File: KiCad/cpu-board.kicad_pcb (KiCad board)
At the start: 2 copper layers, 100 x 100 mm, 25 parts, among them CON1 BARREL_JACK, P1 CONN_01X06, SW1 SW_PUSH_SMALL, SW2 SWITCH_INV, U1 68008D, U2 XC9572XL_VQ44, U3 29F040B, U4 BS62LV4006, X1 OSCILLATOR

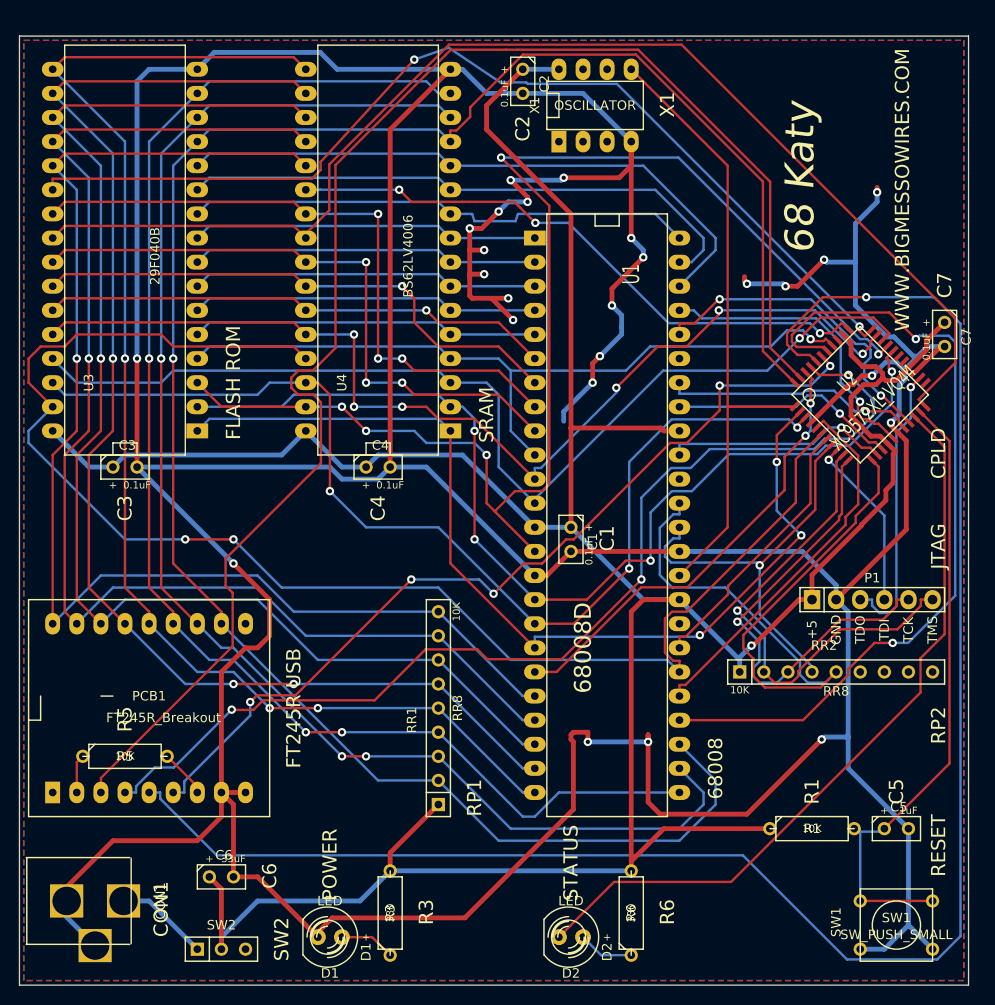
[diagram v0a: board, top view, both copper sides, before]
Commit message: add footprints to schema, add chips to board layout
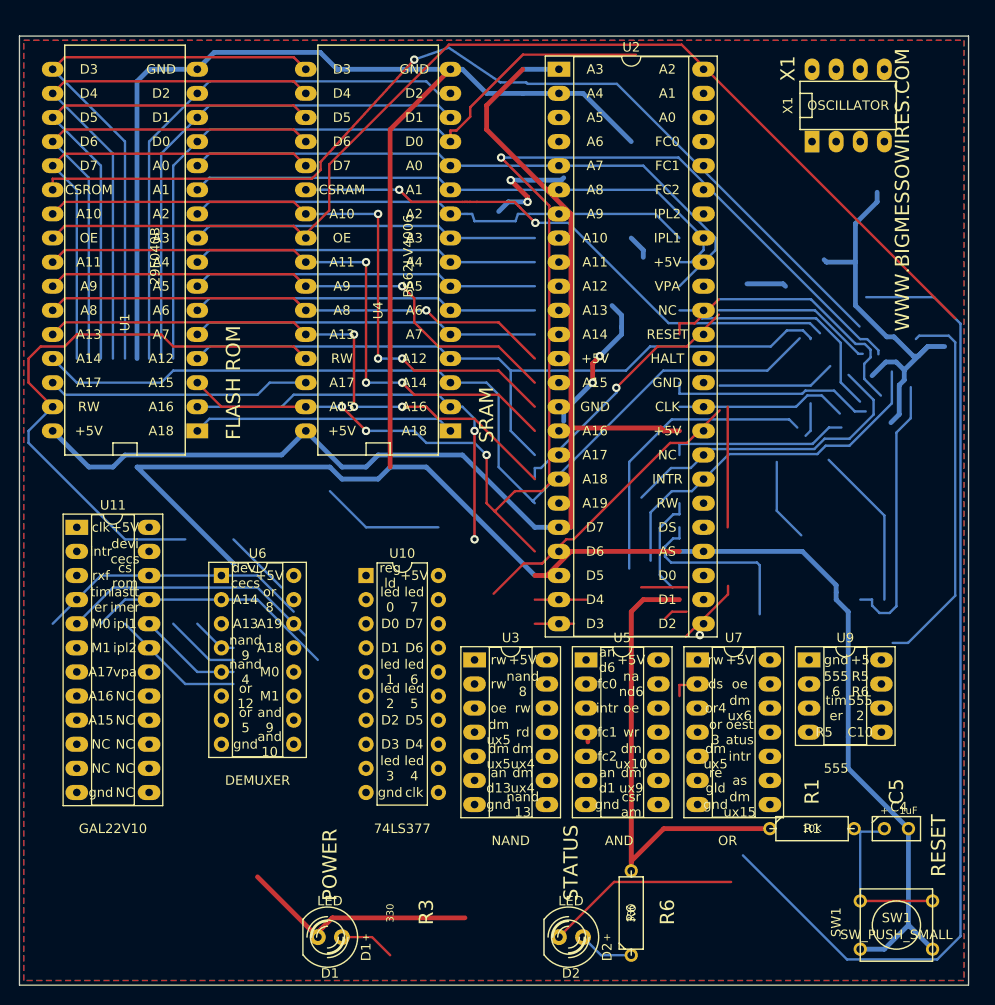
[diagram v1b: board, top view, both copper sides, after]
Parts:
- removed C1, C2, C3, C7: 0.1uF, Discret:C1
- removed the C4 at (97.8, 105.4)
- removed C6: 33uF, Discret:C1
- removed CON1: BARREL_JACK, BMOW:BMOW_BARREL_JACK
- removed P1: CONN_01X06, Pin_Headers:Pin_Header_Straight_1x06
- removed PCB1: FT245R_Breakout, BMOW:FT245_Breakout
- removed R3: 330, Discret:R3-5
- removed R5: 10K, Discret:R3-5
- removed RR1, RR2: RR8, Discret:r_pack8
- removed SW2: SWITCH_INV, Discret:MICROSWITCH_SPST
- removed the U1 at (121.9, 110.5)
- added U10: 74LS377, 68KatyClone:74LS377, F.Cu at (96.5, 116.8)
- added U11: GAL22V10, 68KatyClone:GAL22V10, F.Cu at (66.0, 111.8)
- added U3: 74LS00, 68KatyClone:DIP-14_W7.62mm_Socket_LongPads, F.Cu at (108.0, 125.7)
- added U5: 74LS08, 68KatyClone:DIP-14_W7.62mm_Socket_LongPads, F.Cu at (119.7, 125.7)
- added U6: 74LS139, 68KatyClone:74LS139, F.Cu at (81.3, 116.8)
- added U7: 74LS32, 68KatyClone:DIP-14_W7.62mm_Socket_LongPads, F.Cu at (131.4, 125.7)
- added U9: LM555, 68KatyClone:DIP-8_W7.62mm_Socket_LongPads, F.Cu at (143.2, 125.7)
- U2: value XC9572XL_VQ44 -> 68008D; footprint SMD_Packages:VQFP-44 -> 68KatyClone:DIP-48_W15.24mm_Socket_LongPads
- moved U2 46.7 mm to (116.8, 63.5), turned to 0 degrees
- moved X1 26.7 mm to (147.3, 67.3)
- renumbered C5 to C4, U3 to U1
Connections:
- C4 pad 1: /BTN -> /RESET
- R1 pad 2: /BTN -> /RESET
- SW1 pad 1: /BTN -> /RESET
- U1 pad 22: /CEROM -> /CSROM
- U2 pad 1: /CLK -> /A3
- U2 pad 10: /TMS -> /A12
- U2 pad 11: /TCK -> /A13
- U2 pad 12: /RESET -> /A14
- U2 pad 13: /VPA -> +5V
- U2 pad 14: /IPL1 -> /A15
- U2 pad 15: +5V -> GND
- U2 pad 16: /FC0 -> /A16
- U2 pad 17: GND -> /A17
- U2 pad 18: /IPL2 -> /A18
- U2 pad 19: /FC1 -> /A19
- U2 pad 2: /A18 -> /A4
- U2 pad 20: /STATUS -> /D7
- U2 pad 21: /BTN -> /D6
- U2 pad 22: /OE -> /D5
- U2 pad 23: Net-(U2-Pad23) -> /D4
- U2 pad 24: /TDO -> /D3
- U2 pad 25: GND -> /D2
- U2 pad 26: +5V -> /D1
- U2 pad 27: Net-(U2-Pad27) -> /D0
- U2 pad 28: Net-(U2-Pad28) -> /AS
- U2 pad 29: /A16 -> /DS
- U2 pad 3: /A17 -> /A5
- U2 pad 30: /A15 -> /RW
- U2 pad 31: /A14 -> /INTR
- U2 pad 32: /A13 -> Net-(U2-Pad32)
- U2 pad 33: /CEROM -> +5V
- U2 pad 34: /CERAM -> /CLK
- U2 pad 35: +5V -> GND
- U2 pad 36: Net-(U2-Pad36) -> /HALT
- U2 pad 37: /A12 -> /RESET
- U2 pad 38: /AS -> Net-(U2-Pad38)
- U2 pad 39: /RD -> /VPA
- U2 pad 4: GND -> /A6
- U2 pad 40: /WR -> +5V
- U2 pad 41: /RXF -> /IPL1
- U2 pad 42: /A19 -> /IPL2
- U2 pad 43: /TXE -> /FC2
- U2 pad 44: /D0 -> /FC1
- U2 pad 5: /DS -> /A7
- U2 pad 6: /RW -> /A8
- U2 pad 7: /DTACK -> /A9
- U2 pad 8: /HALT -> /A10
- U2 pad 9: /TDI -> /A11
- U4 pad 22: /CERAM -> /CSRAM
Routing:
- net GND: track 618.6 -> 349.5 mm, vias 25 -> 2
- net /WR: track 184.8 -> 0.00 mm, vias 1 -> 0
- net /TXE: track 160.0 -> 0.00 mm
- net /D0: track 218.9 -> 76.2 mm, vias 1 -> 0
- net +5V: track 329.1 -> 189.7 mm, vias 1 -> 0
- net /RXF: track 111.2 -> 0.00 mm, vias 3 -> 0
- net /CEROM: track 106.4 -> 0.00 mm, vias 2 -> 0
- net /CSROM: track 0.00 -> 104.1 mm, vias 0 -> 1
- net Net-(U11-Pad13): track 0.00 -> 104.1 mm
- net /D1: track 152.4 -> 54.7 mm, vias 3 -> 0
- net /RD: track 93.5 -> 0.00 mm, vias 5 -> 0
- net /D2: track 149.6 -> 57.8 mm, vias 3 -> 0
- net /D7: track 136.3 -> 49.1 mm, vias 1 -> 0
- net /D6: track 137.3 -> 52.2 mm, vias 1 -> 0
- net /D5: track 138.4 -> 55.2 mm, vias 1 -> 0
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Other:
- board text added: "+5V"
- board text added: "555"
- board text added: "555 2"
- board text added: "555 6"
- board text added: "74LS377"
- board text added: "A0"
- board text added: "A1"
- board text added: "A10"
- board text added: "A11"
- board text added: "A12"
- board text added: "A13"
- board text added: "A14"
- board text added: "A15"
- board text added: "A16"
- board text added: "A17"
- board text added: "A18"
- board text added: "A19"
- board text added: "A2"
- board text added: "A3"
- board text added: "A4"
- board text added: "A5"
- board text added: "A6"
- board text added: "A7"
- board text added: "A8"
- board text added: "A9"
- board text added: "AND"
- board text added: "AS"
- board text added: "C10"
- board text added: "CLK"
- board text added: "CSRAM"
- board text added: "CSROM"
- board text added: "D0"
- board text added: "D3"
- board text added: "D4"
- board text added: "D5"
- board text added: "D6"
- board text added: "D7"
- board text added: "DEMUXER"
- board text added: "DS"
- board text added: "FC0"
- board text added: "FC1"
- board text added: "FC2"
- board text added: "GAL22V10"
- board text added: "HALT"
- board text added: "INTR"
- board text added: "IPL1"
- board text added: "IPL2"
- board text added: "M0"
- board text added: "M1"
- board text added: "NAND"
- board text added: "NC"
- board text added: "OE"
- board text added: "OR"
- board text added: "R5 R6"
- board text added: "RW"
- board text added: "VPA"
- board text added: "an d1"
- board text added: "an d13"
- board text added: "an d6"
- board text added: "and 10"
- board text added: "and 9"
- board text added: "as"
- board text added: "clk"
- board text added: "cs rom"
- board text added: "csr am"
- board text added: "devi cecs"
- board text added: "dm ux10"
- board text added: "dm ux15"
- board text added: "dm ux4"
- board text added: "dm ux5"
- board text added: "dm ux6"
- board text added: "dm ux9"
- board text added: "ds"
- board text added: "fc0"
- board text added: "fc1"
- board text added: "fc2"
- board text added: "gnd"
- board text added: "intr"
- board text added: "ipl1"
- board text added: "ipl2"
- board text added: "lastt imer"
- board text added: "led 0"
- board text added: "led 1"
- board text added: "led 2"
- board text added: "led 3"
- board text added: "led 4"
- board text added: "led 5"
- board text added: "led 6"
- board text added: "led 7"
- board text added: "na nd6"
- board text added: "nand 13"
- board text added: "nand 4"
- board text added: "nand 8"
- board text added: "nand 9"
- board text added: "oe"
- board text added: "oest atus"
- board text added: "or 12"
- board text added: "or 3"
- board text added: "or 5"
- board text added: "or 8"
- board text added: "or4"
- board text added: "rd"
- board text added: "re gld"
- board text added: "reg ld"
- board text added: "rw"
- board text added: "rxf"
- board text added: "tim er"
- board text added: "vpa"
- board text added: "wr"
- board text removed: "0.1uF"
- board text removed: "33uF"
- board text removed: "68 Katy"
- board text removed: "68008"
- board text removed: "C1"
- board text removed: "C2"
- board text removed: "C3"
- board text removed: "C4"
- board text removed: "C6"
- board text removed: "C7"
- board text removed: "CON1"
- board text removed: "CPLD"
- board text removed: "FT245R USB"
- board text removed: "JTAG"
- board text removed: "RP1"
- board text removed: "RP2"
- board text removed: "SW2"
- board text removed: "TCK"
- board text removed: "TDI"
- board text removed: "TDO"
- board text removed: "TMS"

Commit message: switch demuxer footprint for long-pad socket, clean up old traces
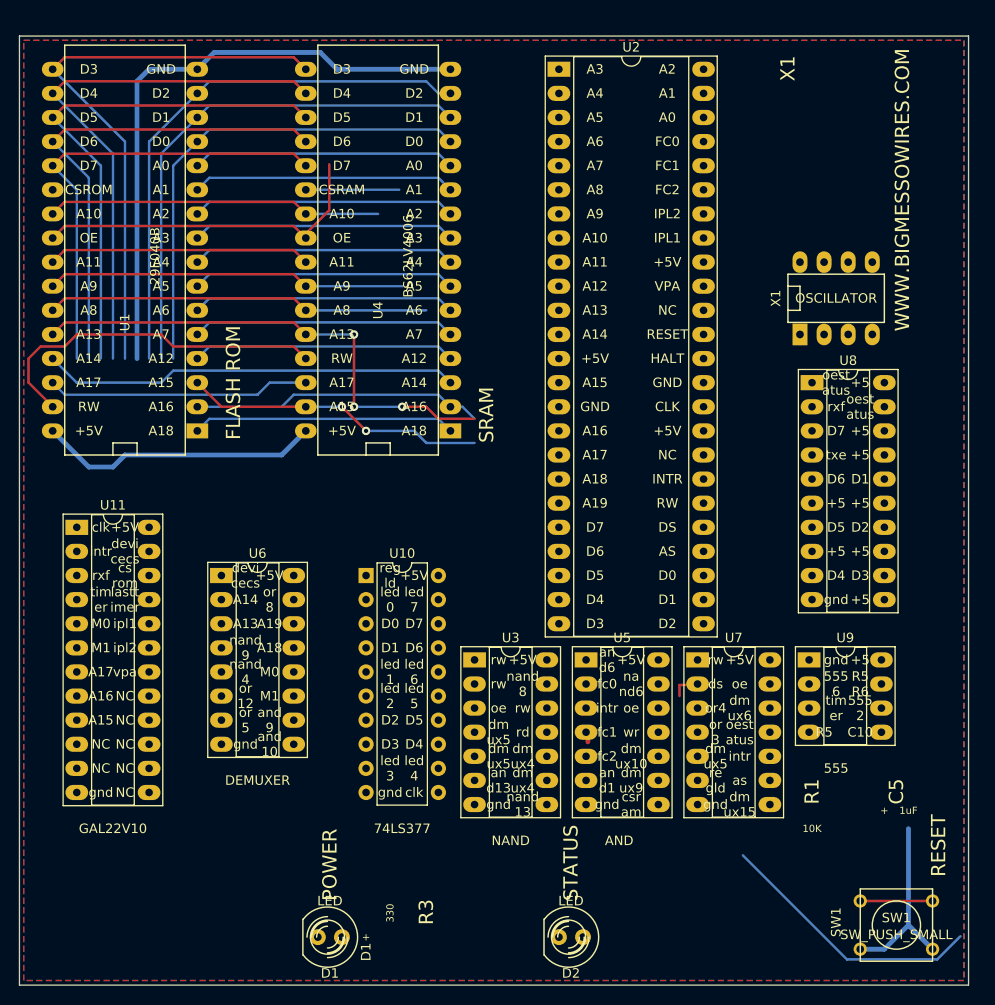
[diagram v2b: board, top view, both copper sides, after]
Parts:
- removed C4: 1uF, Discret:C1
- removed R1: 10K, Discret:R3-5
- removed R6: 330, Discret:R3-5
- added U8: 74LS244, 68KatyClone:DIP-20_W7.62mm_Socket_LongPads, F.Cu at (143.5, 96.5)
- U6: footprint 68KatyClone:74LS139 -> 68KatyClone:DIP-16_W7.62mm_Socket_LongPads
- moved X1 20.4 mm to (146.1, 87.6)
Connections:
- U3 pad 14: +5V -> (no net)
- U5 pad 14: +5V -> (no net)
- U7 pad 14: +5V -> (no net)
- U7 pad 7: GND -> (no net)
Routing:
- net GND: track 349.5 -> 84.1 mm, vias 2 -> 0
- net +5V: track 189.7 -> 29.8 mm
- net /A15: track 182.5 -> 31.8 mm, vias 5 -> 2
- net /CSROM: track 104.1 -> 0.00 mm, vias 1 -> 0
- net /OE: track 121.4 -> 38.2 mm
- net Net-(U11-Pad13): track 104.1 -> 28.5 mm
- net /A12: track 100.2 -> 27.7 mm
- net /A14: track 97.9 -> 44.0 mm
- net /CSRAM: track 60.4 -> 9.85 mm, vias 2 -> 0
- net /DEVICECS: track 48.1 -> 0.00 mm
- net /RW: track 85.0 -> 37.4 mm, vias 2 -> 0
- net /AS: track 39.9 -> 0.00 mm
- net /A11: track 66.7 -> 27.7 mm, vias 3 -> 0
- net /INTR: track 38.6 -> 0.00 mm
- net /A0: track 65.5 -> 27.7 mm
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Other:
- board text added: "txe"
- board text removed: "OR"
- board text removed: "R6"

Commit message: fix errors in PCB pin labels
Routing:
- net Net-(D4-Pad2): track 1.81 -> 0.00 mm
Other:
- board text added: "OR"
- board text added: "dm ux7"
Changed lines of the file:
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@@
   (general
     (thickness 1.6)
-    (drawings 269)
-    (tracks 165)
+    (drawings 270)
+    (tracks 163)
     (zones 0)
     (modules 15)
@@
     (pad_to_mask_clearance 0)
     (aux_axis_origin 0 0)
-    (visible_elements 7FFCFFFF)
+    (visible_elements 7FFCF7FF)
     (pcbplotparams
       (layerselection 0x010f0_80000001)
@@
       (net 1 GND))
   )
+  (gr_text OR (at 134.62 144.78) (layer F.SilkS)
+    (effects (font (size 1 1) (thickness 0.15)))
+  )
   (gr_text 74LS377 (at 100.33 143.51) (layer F.SilkS)
     (effects (font (size 1 1) (thickness 0.15)))
@@
     (effects (font (size 1 1) (thickness 0.15)))
   )
-  (gr_text +5 (at 148.59 101.6) (layer F.SilkS)
+  (gr_text D0 (at 148.59 101.6) (layer F.SilkS)
     (effects (font (size 1 1) (thickness 0.15)))
   )
@@
     (effects (font (size 1 1) (thickness 0.15)))
   )
-  (gr_text "dm\nux5" (at 133.35 135.89) (layer F.SilkS)
+  (gr_text "dm\nux7" (at 133.35 135.89) (layer F.SilkS)
     (effects (font (size 1 1) (thickness 0.15)))
   )
@@
   (segment (start 100.0131 76.1908) (end 91.7035 76.1908) (width 0.254) (layer B.Cu) (net 51))
   (segment (start 91.7035 76.1908) (end 91.6943 76.2) (width 0.254) (layer B.Cu) (net 51))
-  (segment (start 129.54 129.54) (end 129.54 128.3713) (width 0.254) (layer F.Cu) (net 67))
-  (segment (start 130.1772 128.3713) (end 129.54 128.3713) (width 0.254) (layer F.Cu) (net 67))
   (segment (start 136.2268 146.3235) (end 147.1942 157.2909) (width 0.254) (layer B.Cu) (net 80))
   (segment (start 147.1942 157.2909) (end 156.7005 157.2909) (width 0.254) (layer B.Cu) (net 80))

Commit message: add some address lines for fun
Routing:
- net GND: track 84.1 -> 129.6 mm
- net /A3: track 27.7 -> 50.7 mm
- net /A7: track 27.7 -> 50.4 mm
- net /A5: track 27.7 -> 50.4 mm
- net /A4: track 27.7 -> 50.4 mm
- net /A6: track 27.7 -> 50.4 mm
- net /OE: track 38.2 -> 29.6 mm
- net /A10: track 35.3 -> 27.7 mm
- net /A11: track 27.7 -> 29.1 mm
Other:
- board text removed: "dm ux7"
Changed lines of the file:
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@@
     (thickness 1.6)
     (drawings 270)
-    (tracks 163)
+    (tracks 188)
     (zones 0)
     (modules 15)
@@
     (pad_to_mask_clearance 0)
     (aux_axis_origin 0 0)
-    (visible_elements 7FFCF7FF)
+    (visible_elements 7FFCFFFF)
     (pcbplotparams
       (layerselection 0x010f0_80000001)
@@
     (effects (font (size 1 1) (thickness 0.15)))
   )
-  (gr_text "dm\nux7" (at 133.35 135.89) (layer F.SilkS)
+  (gr_text "dm\nux5" (at 133.35 135.89) (layer F.SilkS)
     (effects (font (size 1 1) (thickness 0.15)))
   )
@@
   (segment (start 93.472 63.5) (end 105.41 63.5) (width 0.508) (layer B.Cu) (net 1))
   (segment (start 78.74 63.5) (end 80.518 61.722) (width 0.508) (layer B.Cu) (net 1))
+  (segment (start 111.76 99.06) (end 116.84 99.06) (width 0.508) (layer B.Cu) (net 1))
+  (segment (start 110.49 97.79) (end 111.76 99.06) (width 0.508) (layer B.Cu) (net 1))
+  (segment (start 110.49 64.77) (end 110.49 97.79) (width 0.508) (layer B.Cu) (net 1))
+  (segment (start 105.41 63.5) (end 109.22 63.5) (width 0.508) (layer B.Cu) (net 1))
+  (segment (start 109.22 63.5) (end 110.49 64.77) (width 0.508) (layer B.Cu) (net 1))
   (segment (start 90.17 101.6) (end 87.63 104.14) (width 0.508) (layer B.Cu) (net 4))
   (segment (start 87.63 104.14) (end 71.12 104.14) (width 0.508) (layer B.Cu) (net 4))
@@
   (segment (start 104.14 80.01) (end 80.01 80.01) (width 0.254) (layer B.Cu) (net 19))
   (segment (start 80.01 80.01) (end 78.74 81.28) (width 0.254) (layer B.Cu) (net 19))
+  (segment (start 105.7656 81.28) (end 109.22 77.8256) (width 0.254) (layer F.Cu) (net 19))
+  (segment (start 105.41 81.28) (end 105.7656 81.28) (width 0.254) (layer F.Cu) (net 19))
+  (segment (start 116.44 63.5) (end 116.84 63.5) (width 0.254) (layer F.Cu) (net 19))
+  (segment (start 109.22 70.72) (end 116.44 63.5) (width 0.254) (layer F.Cu) (net 19))
+  (segment (start 109.22 77.8256) (end 109.22 70.72) (width 0.254) (layer F.Cu) (net 19))
   (segment (start 105.41 83.82) (end 104.14 82.55) (width 0.254) (layer B.Cu) (net 20))
   (segment (start 104.14 82.55) (end 80.01 82.55) (width 0.254) (layer B.Cu) (net 20))
   (segment (start 80.01 82.55) (end 78.74 83.82) (width 0.254) (layer B.Cu) (net 20))
+  (segment (start 105.7656 83.82) (end 110.49 79.0956) (width 0.254) (layer F.Cu) (net 20))
+  (segment (start 105.41 83.82) (end 105.7656 83.82) (width 0.254) (layer F.Cu) (net 20))
+  (segment (start 110.49 79.0956) (end 110.49 72.39) (width 0.254) (layer F.Cu) (net 20))
+  (segment (start 110.49 72.39) (end 116.84 66.04) (width 0.254) (layer F.Cu) (net 20))
   (segment (start 105.41 86.36) (end 104.14 85.09) (width 0.254) (layer B.Cu) (net 21))
   (segment (start 104.14 85.09) (end 80.01 85.09) (width 0.254) (layer B.Cu) (net 21))
   (segment (start 80.01 85.09) (end 78.74 86.36) (width 0.254) (layer B.Cu) (net 21))
+  (segment (start 105.7656 86.36) (end 111.76 80.3656) (width 0.254) (layer F.Cu) (net 21))
+  (segment (start 105.41 86.36) (end 105.7656 86.36) (width 0.254) (layer F.Cu) (net 21))
+  (segment (start 111.76 80.3656) (end 111.76 73.66) (width 0.254) (layer F.Cu) (net 21))
+  (segment (start 115.48101 69.93899) (end 116.84 68.58) (width 0.254) (layer F.Cu) (net 21))
+  (segment (start 111.76 73.66) (end 115.48101 69.93899) (width 0.254) (layer F.Cu) (net 21))
   (segment (start 105.41 88.9) (end 104.14 87.63) (width 0.254) (layer B.Cu) (net 22))
   (segment (start 104.14 87.63) (end 80.01 87.63) (width 0.254) (layer B.Cu) (net 22))
   (segment (start 80.01 87.63) (end 78.74 88.9) (width 0.254) (layer B.Cu) (net 22))
+  (segment (start 105.7656 88.9) (end 113.03 81.6356) (width 0.254) (layer F.Cu) (net 22))
+  (segment (start 105.41 88.9) (end 105.7656 88.9) (width 0.254) (layer F.Cu) (net 22))
+  (segment (start 113.03 81.6356) (end 113.03 74.93) (width 0.254) (layer F.Cu) (net 22))
+  (segment (start 113.03 74.93) (end 116.84 71.12) (width 0.254) (layer F.Cu) (net 22))
   (segment (start 105.41 91.44) (end 104.14 90.17) (width 0.254) (layer B.Cu) (net 23))
   (segment (start 104.14 90.17) (end 80.01 90.17) (width 0.254) (layer B.Cu) (net 23))
   (segment (start 80.01 90.17) (end 78.74 91.44) (width 0.254) (layer B.Cu) (net 23))
+  (segment (start 105.7656 91.44) (end 114.3 82.9056) (width 0.254) (layer F.Cu) (net 23))
+  (segment (start 105.41 91.44) (end 105.7656 91.44) (width 0.254) (layer F.Cu) (net 23))
+  (segment (start 114.3 82.9056) (end 114.3 76.2) (width 0.254) (layer F.Cu) (net 23))
+  (segment (start 114.3 76.2) (end 116.84 73.66) (width 0.254) (layer F.Cu) (net 23))
   (segment (start 90.17 88.9) (end 88.9 87.63) (width 0.254) (layer F.Cu) (net 24))
   (segment (start 88.9 87.63) (end 64.77 87.63) (width 0.254) (layer F.Cu) (net 24))
@@
   (segment (start 88.9 77.47) (end 64.77 77.47) (width 0.254) (layer F.Cu) (net 26))
   (segment (start 64.77 77.47) (end 63.5 78.74) (width 0.254) (layer F.Cu) (net 26))
-  (segment (start 90.17 78.74) (end 97.79 78.74) (width 0.254) (layer B.Cu) (net 26))
   (segment (start 90.17 83.82) (end 88.9 82.55) (width 0.254) (layer F.Cu) (net 27))
   (segment (start 88.9 82.55) (end 64.77 82.55) (width 0.254) (layer F.Cu) (net 27))
   (segment (start 64.77 82.55) (end 63.5 83.82) (width 0.254) (layer F.Cu) (net 27))
+  (segment (start 90.17 83.82) (end 91.567 83.82) (width 0.254) (layer F.Cu) (net 27))
   (segment (start 105.41 93.98) (end 104.14 92.71) (width 0.254) (layer B.Cu) (net 28))
   (segment (start 104.14 92.71) (end 80.01 92.71) (width 0.254) (layer B.Cu) (net 28))
@@
   (segment (start 80.01 77.47) (end 78.74 78.74) (width 0.254) (layer B.Cu) (net 46))
   (segment (start 139.8458 128.1242) (end 137.9737 128.1242) (width 0.254) (layer B.Cu) (net 47))
-  (segment (start 89.9472 81.0572) (end 92.6419 78.3625) (width 0.254) (layer F.Cu) (net 47))
-  (segment (start 92.6419 78.3625) (end 92.6419 73.5214) (width 0.254) (layer F.Cu) (net 47))
   (segment (start 89.9472 81.0572) (end 88.9 80.01) (width 0.254) (layer F.Cu) (net 47))
   (segment (start 88.9 80.01) (end 64.77 80.01) (width 0.254) (layer F.Cu) (net 47))
